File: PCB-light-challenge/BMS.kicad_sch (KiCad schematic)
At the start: 0 parts

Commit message: Batterij charger foorprint en symbol toegevoegd, BMS schema getekend , LDO symbol en footprint toegevoegd
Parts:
- added C1: 100n, Capacitor_SMD:C_0603_1608Metric, symbol Device:C
- added R1: 330, Resistor_SMD:R_0603_1608Metric, symbol Device:R
- added R2: 2K7, Resistor_SMD:R_0603_1608Metric, symbol Device:R
- added U2: AP9101CK, Package_TO_SOT_SMD:SOT-23-5, symbol Battery_Management:AP9101CK
- added U3: SP8K32FRATB, SOIC127P600X175-8N, symbol SP8K32FRATB:SP8K32FRATB
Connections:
- new net: C1.1, R1.2, U2.2 (VDD)
- new net: R2.1, U2.1 (VM)
- new net: U2.5 (CO), U3.4
- new net: U3.5, U3.7
- new net: U2.4 (DO), U3.2
- new net BAT+: R1.1
- new net GND: C1.2, U2.3 (VSS), U3.1
- new net P-: R2.2, U3.3

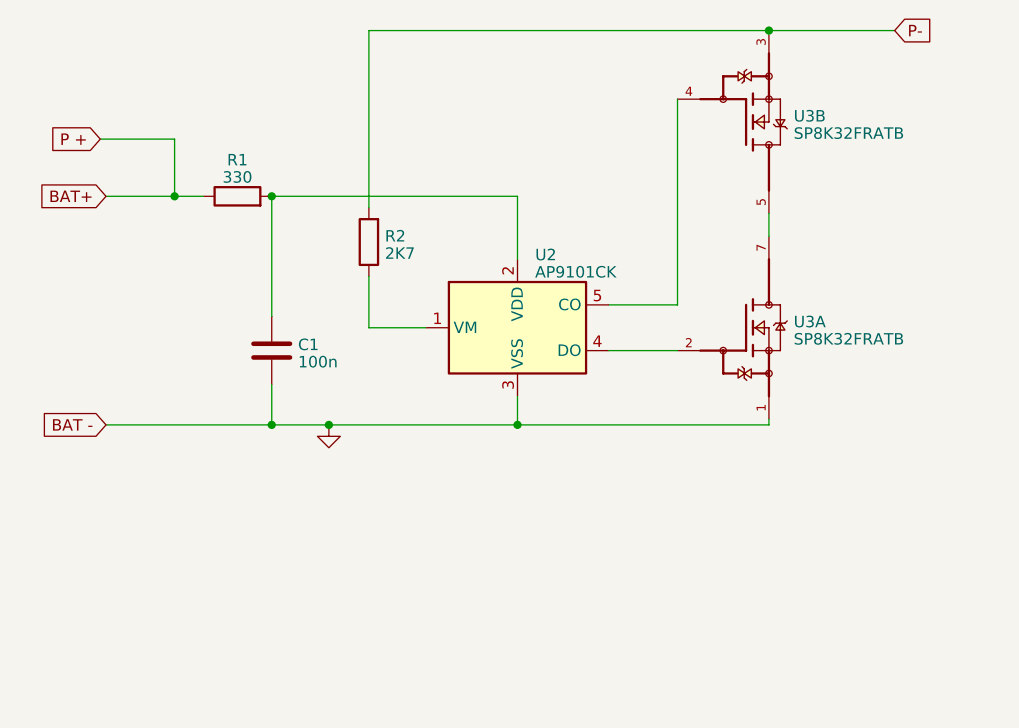
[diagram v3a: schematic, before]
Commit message: RP2040  pinout toegevoegd   met naam
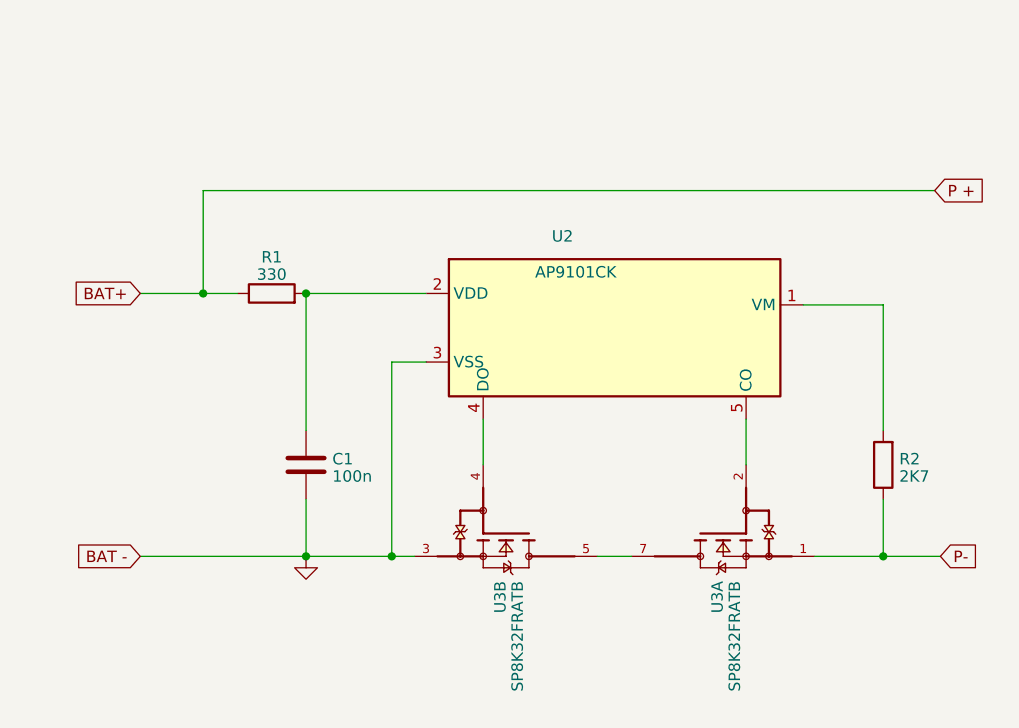
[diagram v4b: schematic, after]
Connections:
- net GND: now also U3.3; no longer U3.1
- net P-: now also R2.1, U3.1; no longer R2.2, U3.3
- net at U2.1 (VM): now also R2.2; no longer R2.1
- net at U3.4: now also U2.4 (DO); no longer U2.5 (CO)
- net at U3.2: now also U2.5 (CO); no longer U2.4 (DO)
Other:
- moved on the sheet: C1, R1, R2, U2, U3A, U3B
